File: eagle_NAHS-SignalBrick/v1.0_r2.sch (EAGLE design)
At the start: 42 parts, among them IC1 ESP12S, IC2 ATTINY212-SSNR, IC3 TP4056, IC4 DW01A, J1 10118194-0001LF, J2 NAHS-BRICK-INTERFACE-V2_B-SIDE, Q1 8205A

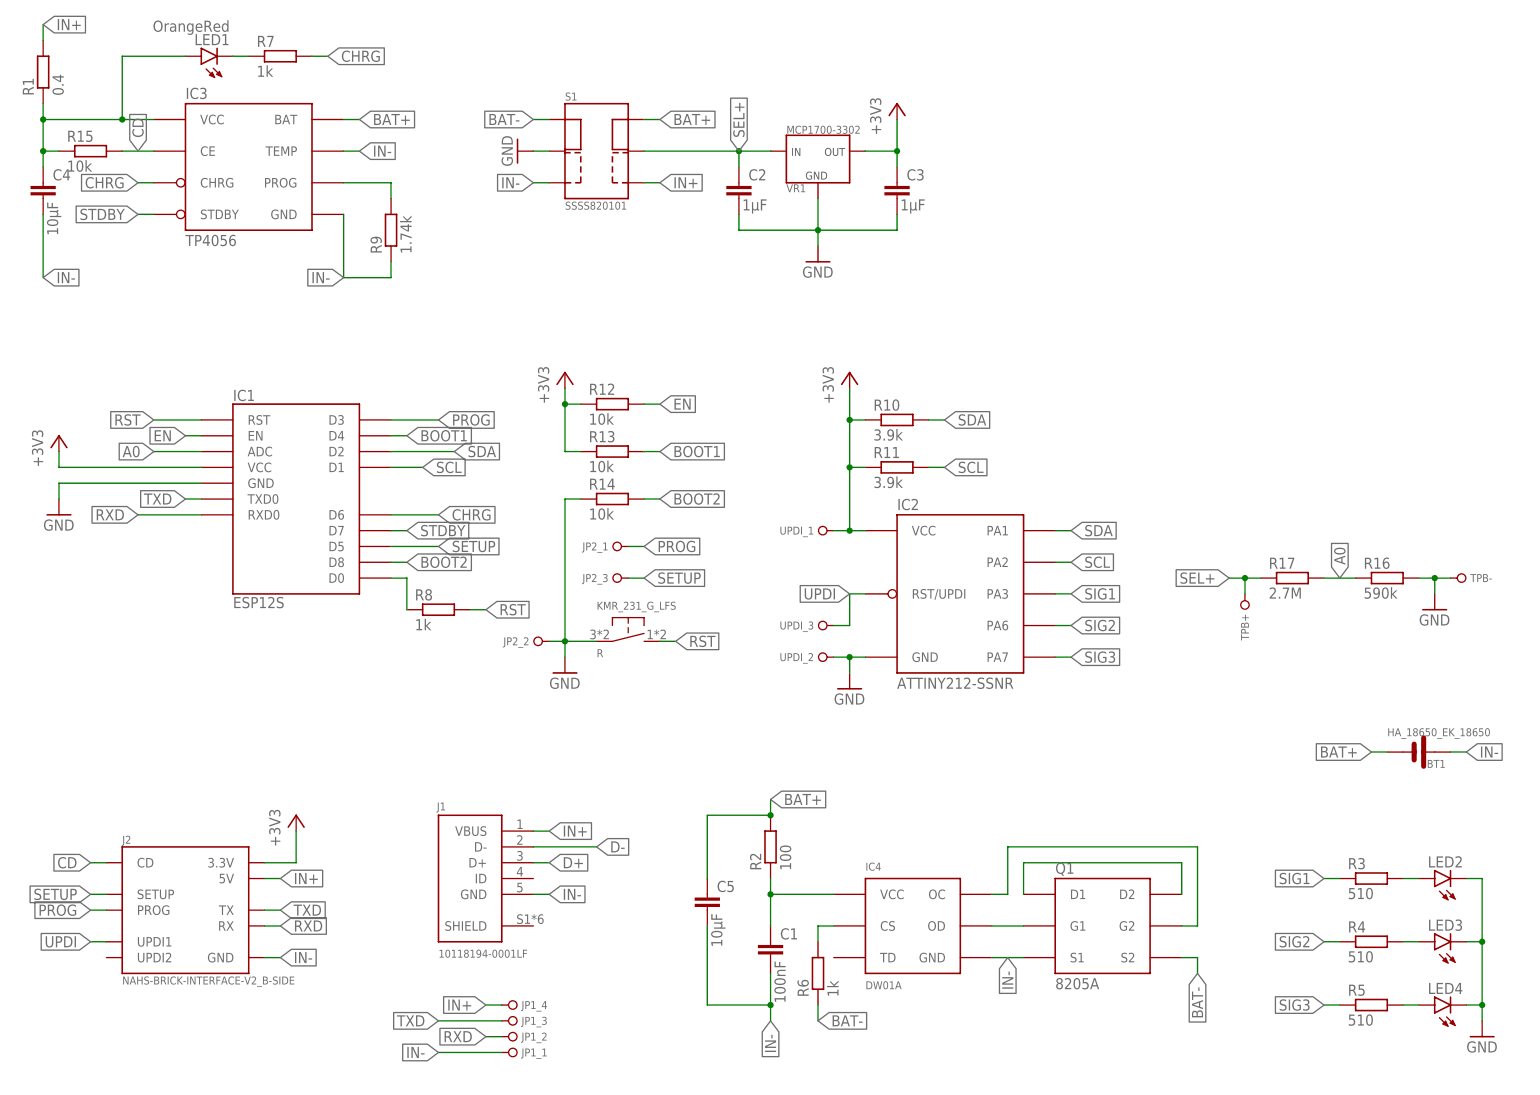
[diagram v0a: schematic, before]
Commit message: Boardlayout v1.0 R2 - Send to JLCPCB
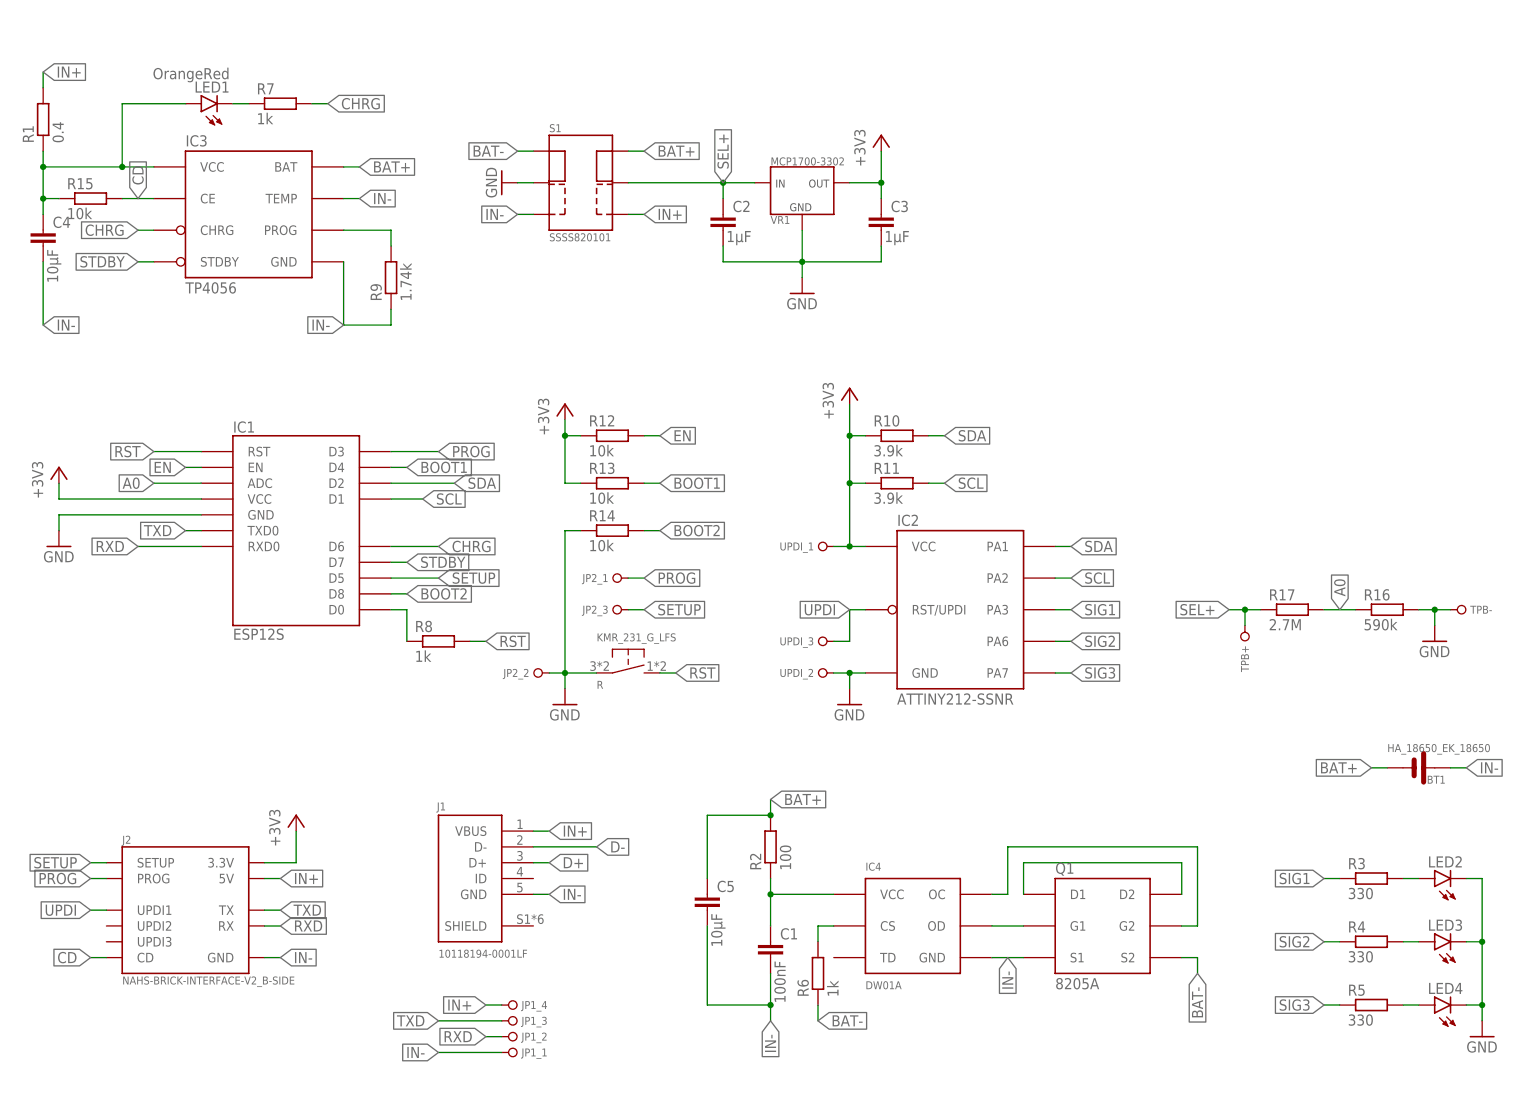
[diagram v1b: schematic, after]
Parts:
- R3, R4, R5: value 510 -> 330
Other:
- moved on the sheet: BT1, C2, C3, C4, IC1, IC2, IC3, JP2_1, JP2_2, JP2_3, LED1, R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
